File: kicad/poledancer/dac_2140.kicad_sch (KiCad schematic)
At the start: 6 parts, among them U4 LM4040AIM3-2.5, U5 AD5328

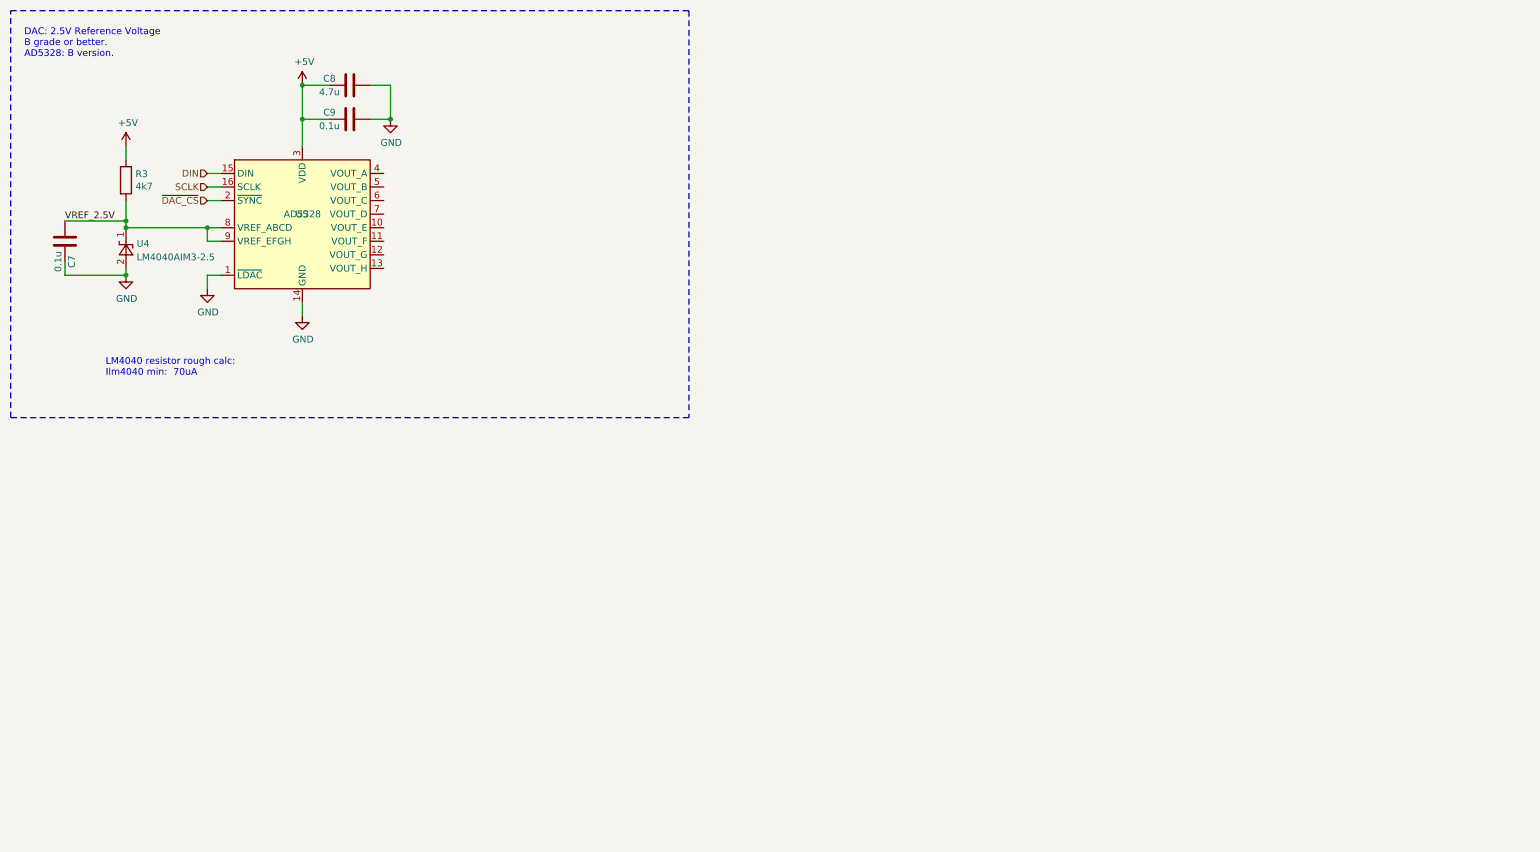
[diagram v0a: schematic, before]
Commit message: schematic about ready for review.  Need GPIO out still.  then review.
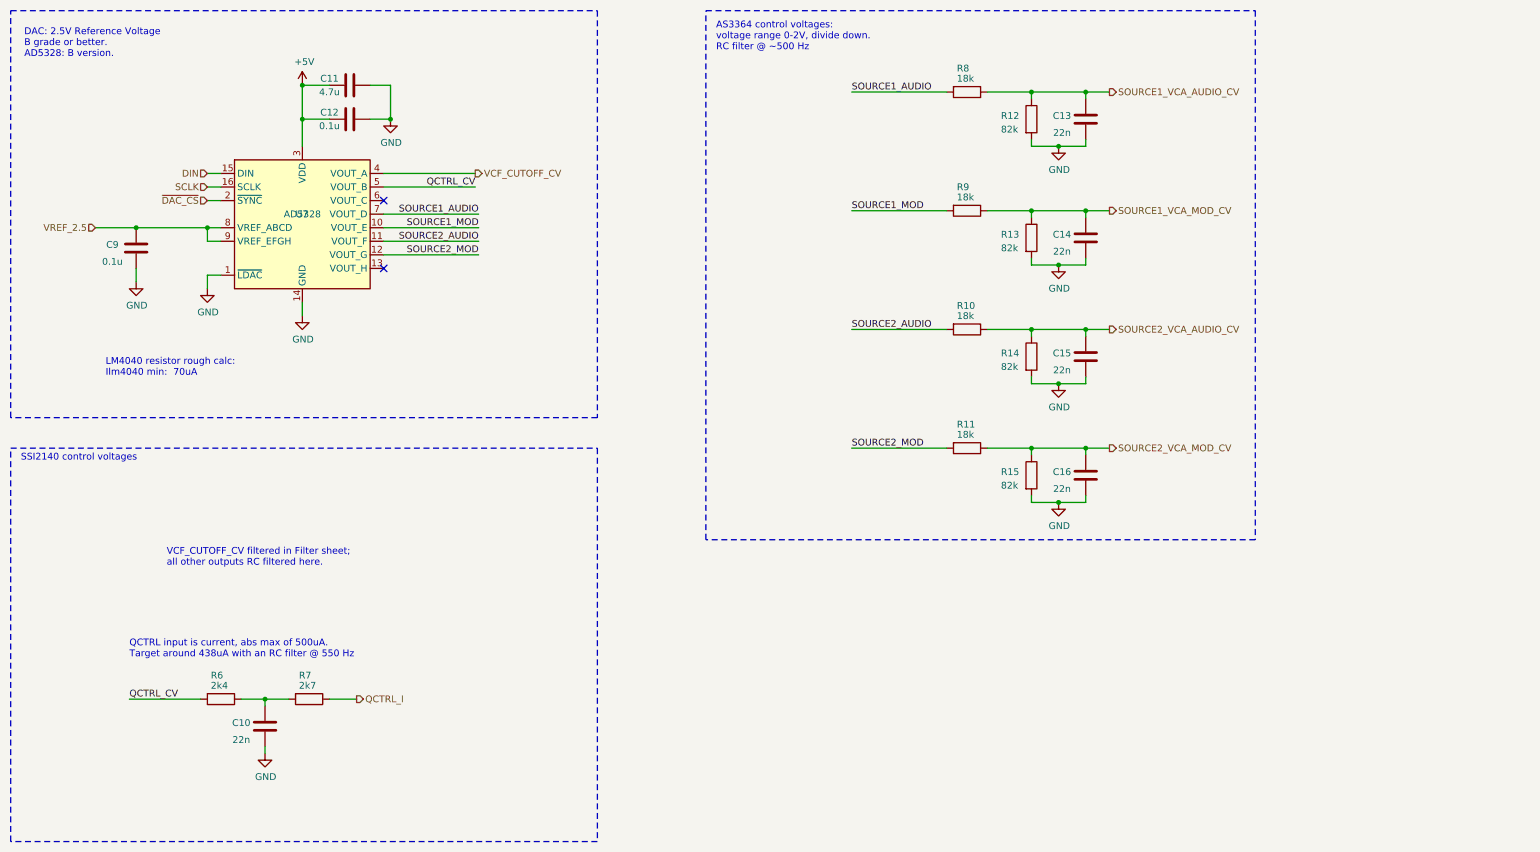
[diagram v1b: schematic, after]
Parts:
- removed R3: 4k7, Resistor_SMD:R_1206_3216Metric, symbol Device:R
- removed U4: LM4040AIM3-2.5, Package_TO_SOT_SMD:SOT-23, symbol Reference_Voltage:LM4040DBZ-2.5
- added C10, C13, C14, C15, C16: 22n, Capacitor_SMD:C_0603_1608Metric, symbol Device:C
- added R10, R11, R8, R9: 18k, Resistor_SMD:R_0603_1608Metric, symbol Device:R
- added R12, R13, R14, R15: 82k, Resistor_SMD:R_0603_1608Metric, symbol Device:R
- added R6: 2k4, Resistor_SMD:R_0603_1608Metric, symbol Device:R
- added R7: 2k7, Resistor_SMD:R_0603_1608Metric, symbol Device:R
- renumbered C8 to C11, C9 to C12, C7 to C9, U5 to U7
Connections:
- net GND: now also C10.2, C13.2, C14.2, C15.2, C16.2, R12.2, R13.2, R14.2, R15.2
- net SOURCE1_MOD: now reaches U7.10 (VOUT_E)
- net SOURCE1_MOD: now also R9.2
- net SOURCE2_AUDIO: now reaches U7.11 (VOUT_F)
- net SOURCE2_AUDIO: now also R10.2
- net SOURCE2_MOD: now reaches U7.12 (VOUT_G)
- net SOURCE2_MOD: now also R11.2
- net VCF_CUTOFF_CV: now reaches U7.4 (VOUT_A)
- net QCTRL_CV: now reaches U7.5 (VOUT_B)
- net QCTRL_CV: now also R6.2
- net SOURCE1_AUDIO: now reaches U7.7 (VOUT_D)
- net SOURCE1_AUDIO: now also R8.2
- net VREF_2.5V renamed VREF_2.5
- new net: C10.1, R6.1, R7.2
- new net QCTRL_I: R7.1
- new net SOURCE1_VCA_AUDIO_CV: C13.1, R12.1, R8.1
- new net SOURCE1_VCA_MOD_CV: C14.1, R13.1, R9.1
- new net SOURCE2_VCA_AUDIO_CV: C15.1, R10.1, R14.1
- new net SOURCE2_VCA_MOD_CV: C16.1, R11.1, R15.1
- no-connect marks 0 -> 2
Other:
- note added: "AS3364 control voltages: voltage range 0-2V, divide down. RC filter @ ~500 Hz"
- note added: "QCTRL input is current, abs max of 500uA. Target around 438uA with an RC filter @ 550 Hz"
- note added: "SSI2140 control voltages"
- note added: "VCF_CUTOFF_CV filtered in Filter sheet; all other outputs RC filtered here."
- company: (none) -> Zoxnoxious Engineering
- title: (none) -> Zoxnoxious Pole Dancer Mixing Filter
- moved on the sheet: C9

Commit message: I wish kicad would warn when things go off-grid
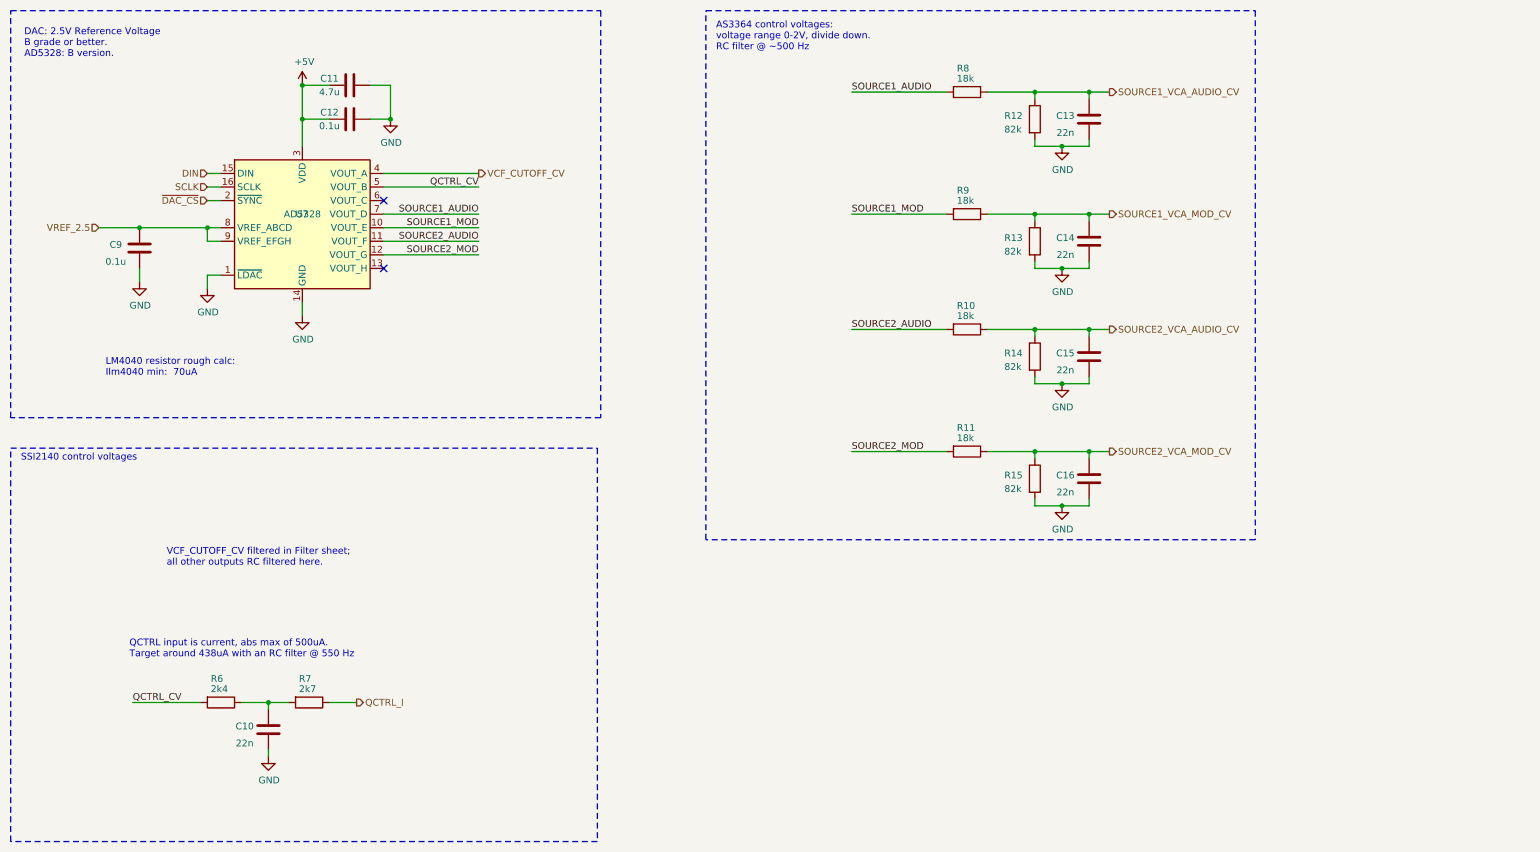
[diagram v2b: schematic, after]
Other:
- moved on the sheet: C10, C13, C14, C15, C16, C9, R11, R12, R13, R14, R15, R6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

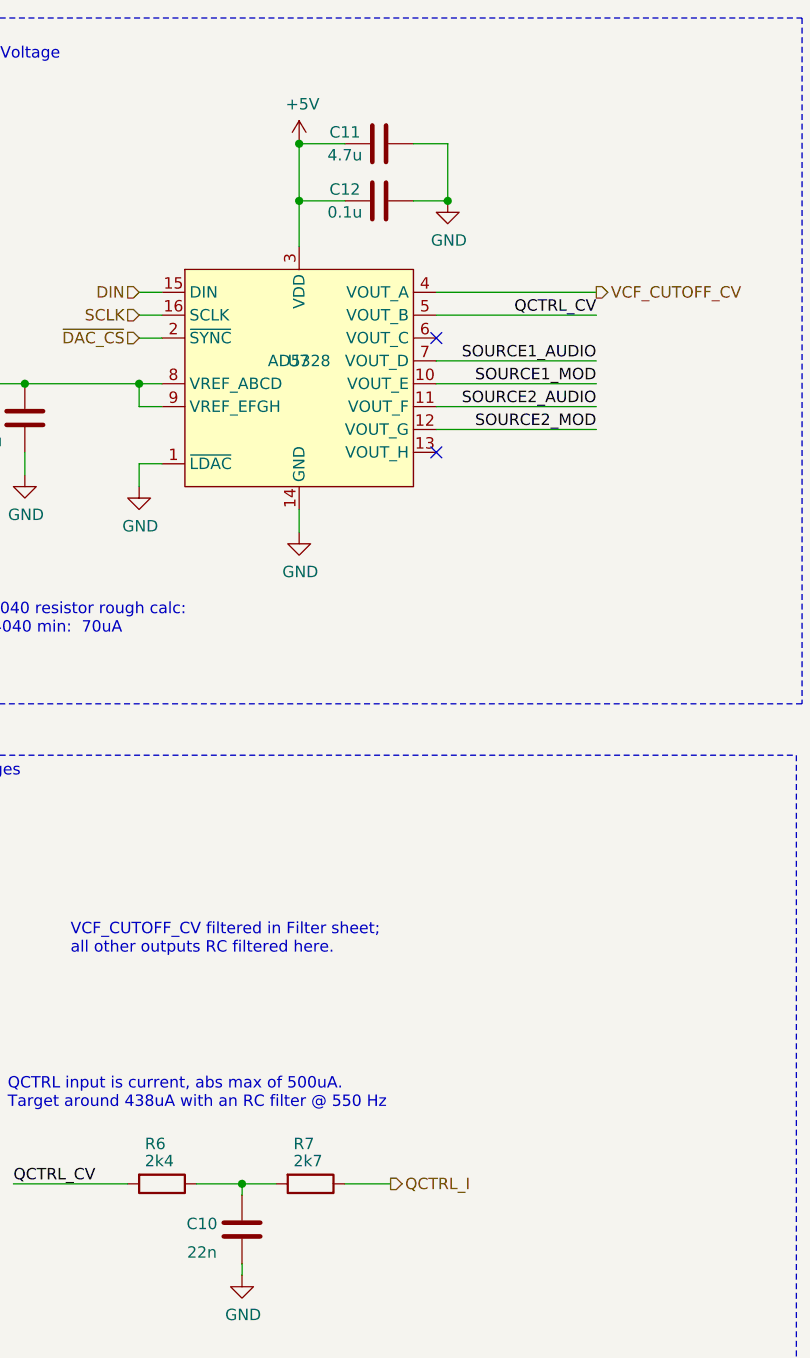
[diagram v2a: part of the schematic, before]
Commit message: ditch moving the VCA cell to last position, keep it in position 2.  More VCA mode offered that way.  Other change is adding all JLCPCB components to fields
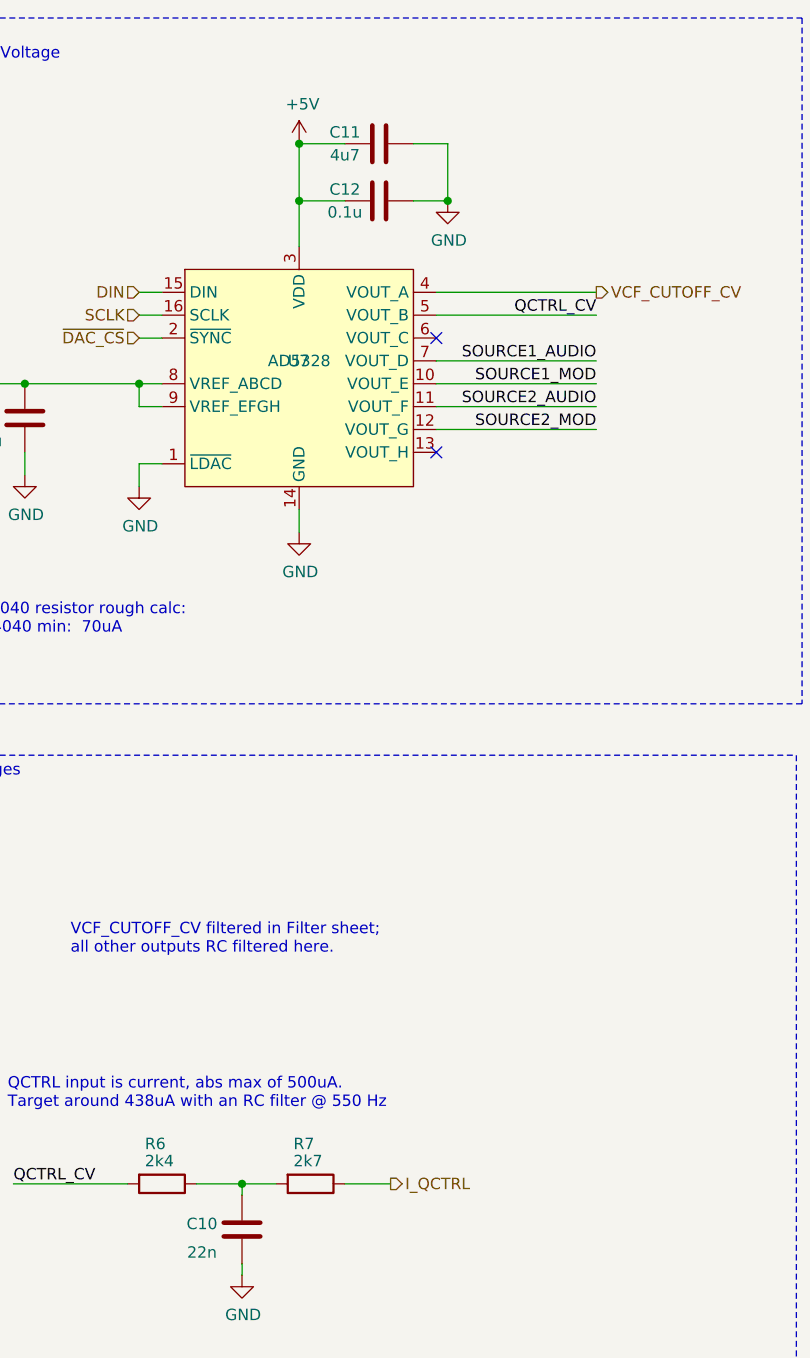
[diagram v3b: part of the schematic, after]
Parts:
- C10, C13, C14, C15, C16: LCSC (none) -> C21122
- C11: value 4.7u -> 4u7; footprint Capacitor_SMD:C_0805_2012Metric -> Capacitor_SMD:C_0603_1608Metric; LCSC (none) -> C19666; LCSC Part C1779 -> (none)
- C12, C9: LCSC (none) -> C14663; LCSC Part C14663 -> (none)
- R10, R11, R8, R9: LCSC (none) -> C25810
- R12, R13, R14, R15: LCSC (none) -> C23254
- R6, R7: LCSC (none) -> C17936; LCSC Part C17936 -> (none)
- U7: LCSC (none) -> C29162; LCSC Part C29162 -> (none)
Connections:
- net QCTRL_I renamed I_QCTRL
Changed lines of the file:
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@@
     (effects (font (size 1.27 1.27)) (justify right))
   )
-  (hierarchical_label "QCTRL_I" (shape output) (at 87.63 149.86 0) (fields_autoplaced)
+  (hierarchical_label "I_QCTRL" (shape output) (at 87.63 149.86 0) (fields_autoplaced)
     (effects (font (size 1.27 1.27)) (justify left))
   )
@@
       (effects (font (size 1.27 1.27)) hide)
     )
-    (property "LCSC Part" "" (at 224.79 107.95 0)
+    (property "LCSC" "C21122" (at 224.79 107.95 0)
       (effects (font (size 1.27 1.27)) hide)
     )
@@
       (effects (font (size 1.27 1.27)) hide)
     )
-    (property "LCSC Part" "" (at 201.93 35.56 0)
+    (property "LCSC" "C25810" (at 201.93 35.56 0)
       (effects (font (size 1.27 1.27)) hide)
     )
@@
       (effects (font (size 1.27 1.27)) hide)
     )
-    (property "LCSC Part" "" (at 201.93 58.42 0)
+    (property "LCSC" "C25810" (at 201.93 58.42 0)
       (effects (font (size 1.27 1.27)) hide)
     )
@@
       (effects (font (size 1.27 1.27)) hide)
     )
-    (property "LCSC Part" "" (at 201.93 102.87 0)
+    (property "LCSC" "C25810" (at 201.93 102.87 0)
       (effects (font (size 1.27 1.27)) hide)
     )
@@
       (effects (font (size 1.27 1.27)) hide)
     )
-    (property "LCSC Part" "" (at 214.63 63.5 0)
+    (property "LCSC" "C23254" (at 214.63 63.5 0)
       (effects (font (size 1.27 1.27)) hide)
     )
@@
       (effects (font (size 1.27 1.27)) hide)
     )
-    (property "LCSC Part" "C14663" (at 46.99 64.77 0)
+    (property "LCSC" "C14663" (at 46.99 64.77 0)
       (effects (font (size 1.27 1.27)) hide)
     )
@@
       (effects (font (size 1.27 1.27)) hide)
     )
-    (property "LCSC Part" "C17936" (at 78.74 149.86 0)
+    (property "LCSC" "C17936" (at 78.74 149.86 0)
       (effects (font (size 1.27 1.27)) hide)
     )
@@
       (effects (font (size 1.27 1.27)) hide)
     )
-    (property "LCSC Part" "" (at 224.79 63.5 0)
+    (property "LCSC" "C21122" (at 224.79 63.5 0)
       (effects (font (size 1.27 1.27)) hide)
     )
@@
       (effects (font (size 1.27 1.27)) hide)
     )
-    (property "LCSC Part" "" (at 214.63 40.64 0)
+    (property "LCSC" "C23254" (at 214.63 40.64 0)
       (effects (font (size 1.27 1.27)) hide)
     )
@@
       (effects (font (size 1.27 1.27)) hide)
     )
-    (property "LCSC Part" "" (at 71.12 154.94 0)
+    (property "LCSC" "C21122" (at 71.12 154.94 0)
       (effects (font (size 1.27 1.27)) hide)
     )
@@
       (effects (font (size 1.27 1.27)))
     )
-    (property "Value" "4.7u" (at 82.55 35.56 90)
-      (effects (font (size 1.27 1.27)))
-    )
-    (property "Footprint" "Capacitor_SMD:C_0805_2012Metric" (at 90.17 33.3248 0)
+    (property "Value" "4u7" (at 82.55 35.56 90)
+      (effects (font (size 1.27 1.27)))
+    )
+    (property "Footprint" "Capacitor_SMD:C_0603_1608Metric" (at 90.17 33.3248 0)
       (effects (font (size 1.27 1.27)) hide)
     )
@@
       (effects (font (size 1.27 1.27)) hide)
     )
-    (property "LCSC Part" "C1779" (at 86.36 34.29 0)
+    (property "LCSC" "C19666" (at 86.36 34.29 0)
       (effects (font (size 1.27 1.27)) hide)
     )
@@
       (effects (font (size 1.27 1.27)) hide)
     )
-    (property "LCSC Part" "C14663" (at 86.36 40.64 0)
+    (property "LCSC" "C14663" (at 86.36 40.64 0)
       (effects (font (size 1.27 1.27)) hide)
     )
@@
       (effects (font (size 1.27 1.27)) hide)
     )
-    (property "LCSC Part" "" (at 224.79 40.64 0)
+    (property "LCSC" "C21122" (at 224.79 40.64 0)
       (effects (font (size 1.27 1.27)) hide)
     )
@@
       (effects (font (size 1.27 1.27)) hide)
     )
-    (property "LCSC Part" "C29162" (at 77.47 58.42 0)
+    (property "LCSC" "C29162" (at 77.47 58.42 0)
       (effects (font (size 1.27 1.27)) hide)
     )
@@
       (effects (font (size 1.27 1.27)) hide)
     )
-    (property "LCSC Part" "" (at 214.63 85.09 0)
+    (property "LCSC" "C23254" (at 214.63 85.09 0)
       (effects (font (size 1.27 1.27)) hide)
     )
@@
       (effects (font (size 1.27 1.27)) hide)
     )
-    (property "LCSC Part" "" (at 224.79 85.09 0)
+    (property "LCSC" "C21122" (at 224.79 85.09 0)
       (effects (font (size 1.27 1.27)) hide)
     )
@@
       (effects (font (size 1.27 1.27)) hide)
     )
-    (property "LCSC Part" "C17936" (at 62.23 149.86 0)
+    (property "LCSC" "C17936" (at 62.23 149.86 0)
       (effects (font (size 1.27 1.27)) hide)
     )
@@
       (effects (font (size 1.27 1.27)) hide)
     )
-    (property "LCSC Part" "" (at 214.63 107.95 0)
+    (property "LCSC" "C23254" (at 214.63 107.95 0)
       (effects (font (size 1.27 1.27)) hide)
     )
@@
       (effects (font (size 1.27 1.27)) hide)
     )
-    (property "LCSC Part" "" (at 201.93 80.01 0)
-      (effects (font (size 1.27 1.27)) hide)
-    )
+    (property "LCSC" "C25810" (at 201.93 80.01 0)
+      (effects (font (size 1.27 1.27)) hide)
+    )
